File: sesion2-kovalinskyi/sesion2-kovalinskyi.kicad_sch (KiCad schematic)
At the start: 0 parts

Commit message: Etapa de alimentacion completada
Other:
- added sheet alimentacion (alimentacion.kicad_sch)
- added sheet microcontrolador (microcontrolador.kicad_sch)
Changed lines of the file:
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@@
 	(generator_version "10.0")
 	(paper "A4")
+	(sheet
+		(at 59.69 95.25)
+		(size 26.67 25.4)
+		(exclude_from_sim no)
+		(in_bom yes)
+		(on_board yes)
+		(dnp no)
+		(fields_autoplaced yes)
+		(stroke
+			(width 0.1524)
+			(type solid)
+		)
+		(fill
+			(color 0 0 0 0)
+		)
+		(property "Sheetname" "microcontrolador"
+			(at 59.69 94.5384 0)
+			(show_name no)
+			(do_not_autoplace no)
+			(effects
+				(font
+					(size 1.27 1.27)
+				)
+				(justify left bottom)
+			)
+		)
+		(property "Sheetfile" "microcontrolador.kicad_sch"
+			(at 59.69 121.2346 0)
+			(show_name no)
+			(do_not_autoplace no)
+			(effects
+				(font
+					(size 1.27 1.27)
+				)
+				(justify left top)
+			)
+		)
+		(instances
+			(project "sesion2-kovalinskyi"
+				(path "/99d4a334-3c53-424d-bcc9-9b696a6ef66c"
+					(page "3")
+				)
+			)
+		)
+	)
+	(sheet
+		(at 60.96 67.31)
+		(size 22.86 19.05)
+		(exclude_from_sim no)
+		(in_bom yes)
+		(on_board yes)
+		(dnp no)
+		(fields_autoplaced yes)
+		(stroke
+			(width 0.1524)
+			(type solid)
+		)
+		(fill
+			(color 0 0 0 0)
+		)
+		(property "Sheetname" "alimentacion"
+			(at 60.96 66.5984 0)
+			(show_name no)
+			(do_not_autoplace no)
+			(effects
+				(font
+					(size 1.27 1.27)
+				)
+				(justify left bottom)
+			)
+		)
+		(property "Sheetfile" "alimentacion.kicad_sch"
+			(at 60.96 86.9446 0)
+			(show_name no)
+			(do_not_autoplace no)
+			(effects
+				(font
+					(size 1.27 1.27)
+				)
+				(justify left top)
+			)
+		)
+		(instances
+			(project "sesion2-kovalinskyi"
+				(path "/99d4a334-3c53-424d-bcc9-9b696a6ef66c"
+					(page "2")
+				)
+			)
+		)
+	)
 	(sheet_instances
 		(path "/"

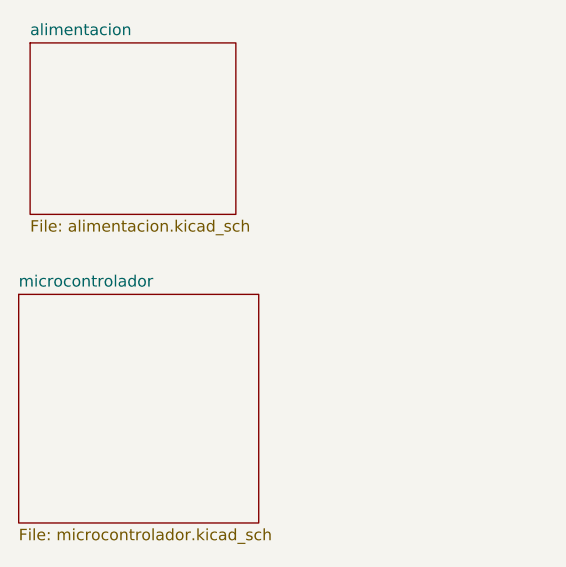
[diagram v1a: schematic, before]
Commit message: Etapa de MCU completada
- MCU
- filtros RC
- resolución ERC con PWR_FLAG
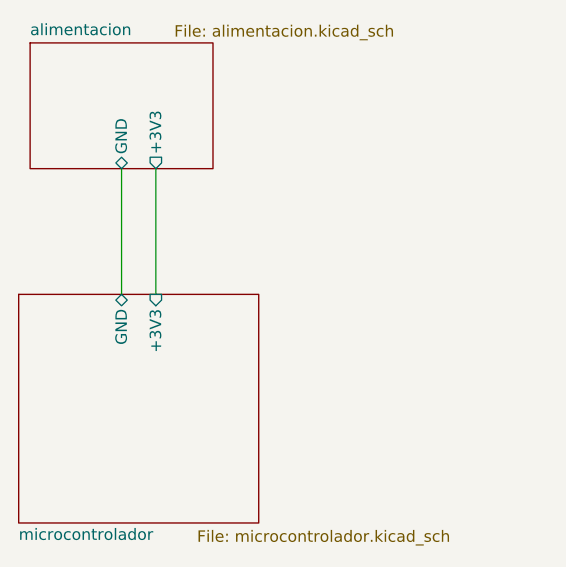
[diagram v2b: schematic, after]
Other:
- sheet alimentacion ports: added +3V3, GND; removed none
- sheet microcontrolador ports: added +3V3, GND; removed none
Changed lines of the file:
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@@
 	(generator_version "10.0")
 	(paper "A4")
+	(wire
+		(pts
+			(xy 71.12 81.28) (xy 71.12 95.25)
+		)
+		(stroke
+			(width 0)
+			(type default)
+		)
+	)
+	(wire
+		(pts
+			(xy 74.93 81.28) (xy 74.93 95.25)
+		)
+		(stroke
+			(width 0)
+			(type default)
+		)
+	)
 	(sheet
 		(at 59.69 95.25)
@@
 		(on_board yes)
 		(dnp no)
-		(fields_autoplaced yes)
 		(stroke
 			(width 0.1524)
@@
 		)
 		(property "Sheetname" "microcontrolador"
-			(at 59.69 94.5384 0)
+			(at 59.69 122.682 0)
 			(show_name no)
 			(do_not_autoplace no)
@@
 		)
 		(property "Sheetfile" "microcontrolador.kicad_sch"
-			(at 59.69 121.2346 0)
+			(at 79.502 121.412 0)
 			(show_name no)
 			(do_not_autoplace no)
@@
 				)
 				(justify left top)
+			)
+		)
+		(pin "+3V3" input
+			(at 74.93 95.25 90)
+			(effects
+				(font
+					(size 1.27 1.27)
+				)
+				(justify right)
+			)
+		)
+		(pin "GND" bidirectional
+			(at 71.12 95.25 90)
+			(effects
+				(font
+					(size 1.27 1.27)
+				)
+				(justify right)
 			)
 		)
@@
 	(sheet
 		(at 60.96 67.31)
-		(size 22.86 19.05)
+		(size 20.32 13.97)
 		(exclude_from_sim no)
 		(in_bom yes)
 		(on_board yes)
 		(dnp no)
-		(fields_autoplaced yes)
 		(stroke
 			(width 0.1524)
@@
 		)
 		(property "Sheetfile" "alimentacion.kicad_sch"
-			(at 60.96 86.9446 0)
+			(at 76.962 65.278 0)
 			(show_name no)
 			(do_not_autoplace no)
@@
 			)
 		)
+		(pin "+3V3" output
+			(at 74.93 81.28 270)
+			(effects
+				(font
+					(size 1.27 1.27)
+				)
+				(justify left)
+			)
+		)
+		(pin "GND" bidirectional
+			(at 71.12 81.28 270)
+			(effects
+				(font
+					(size 1.27 1.27)
+				)
+				(justify left)
+			)
+		)

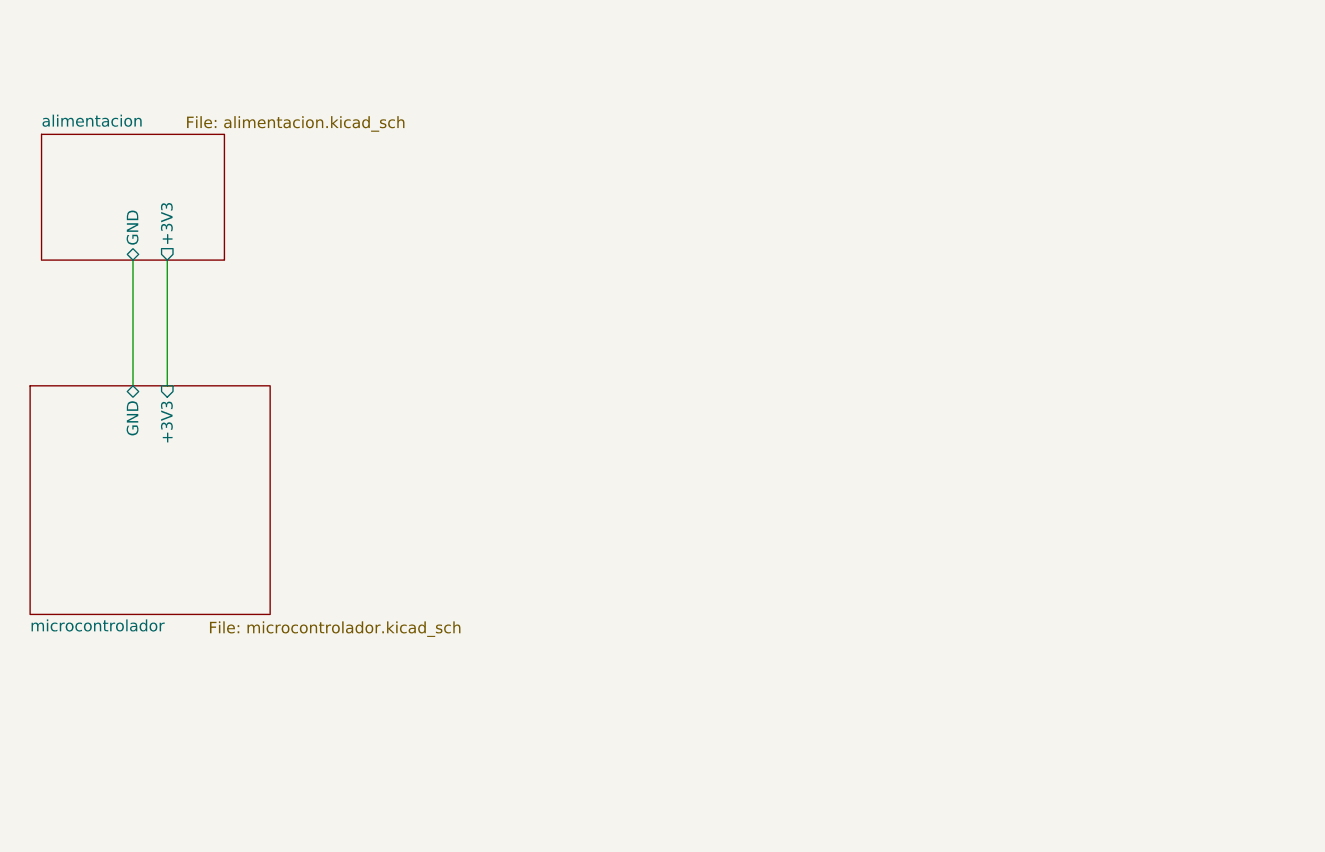
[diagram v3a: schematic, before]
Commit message: Calculo de impedancia y enrutado SPI e I2C
- I2C enrutado en Capa 3 (Stripline) con meandros (regla 3W) y desacoplo C8 pegado a los pines.
- SPI en Capa 1 con ajuste de longitud en SCK, MOSI y MISO (~25,35 mm) y puente en Capa 3 para SPI_CS.
- Validada la integridad de señal en los buses; líneas de datos libres de errores DRC.
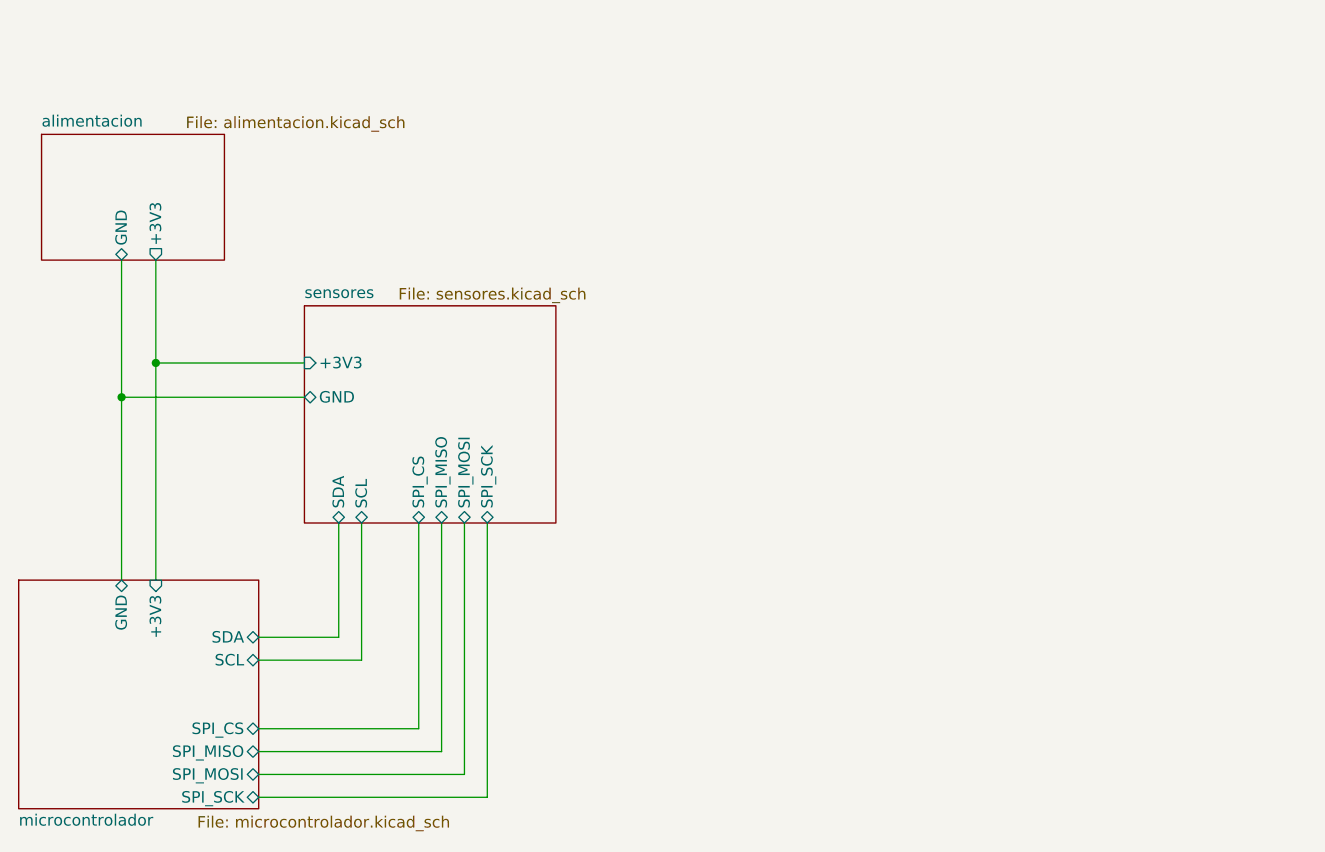
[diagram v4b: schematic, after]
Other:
- added sheet sensores (sensores.kicad_sch)
- sheet microcontrolador ports: added SCL, SDA, SPI_CS, SPI_MISO, SPI_MOSI, SPI_SCK; removed none

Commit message: Sesión 4 - Entrega Completa
- Incorporación de dos sensores en el circuito: uno bajo protocolo I2C y otro bajo protocolo SPI.
- Integración física y esquemática de conector tipo USB-C para comunicación diferencial.
- Integrado bloque USB-C con CH340C y resuelto ERC (conectado el pin V3 a +3V3 según especifica el datasheet para operación a 3,3 V, excluyendo el falso positivo de conflicto de salidas de alimentación del ERC).
- Ajuste de par diferencial (DIFF_90): el uso directo de la herramienta "Tune Skew of Differential Pair" no computa la longitud total completa de las redes al existir saltos de vía y pistas auxiliares en el conector; por ello, el ajuste de longitud se ha resuelto mediante meandros manuales y la definición de reglas personalizadas para la verificación del skew intracanal (< 0.05 mm) en el DRC.
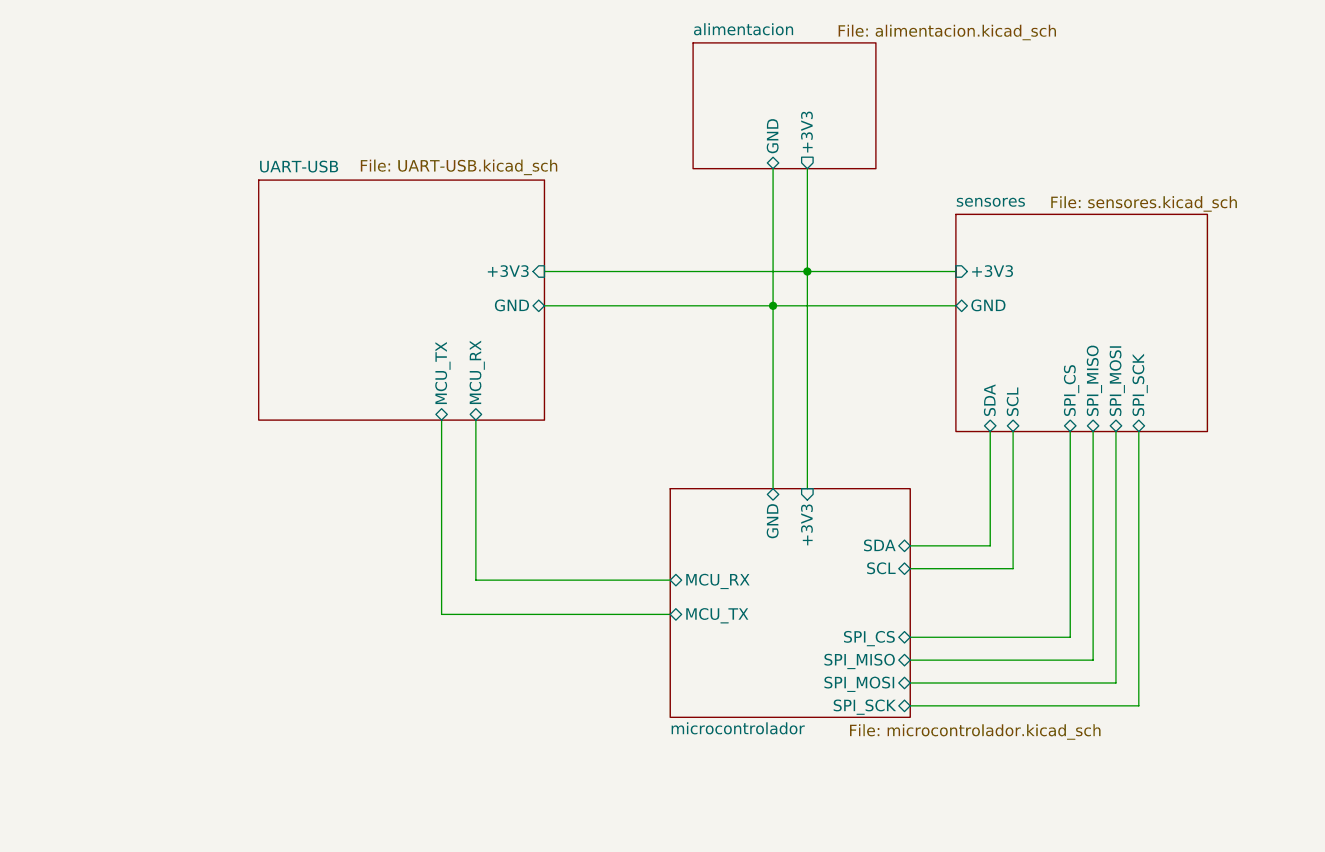
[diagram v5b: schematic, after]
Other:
- added sheet UART-USB (UART-USB.kicad_sch)
- sheet microcontrolador ports: added MCU_RX, MCU_TX; removed none
